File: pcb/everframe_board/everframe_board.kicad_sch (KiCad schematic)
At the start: 4 parts

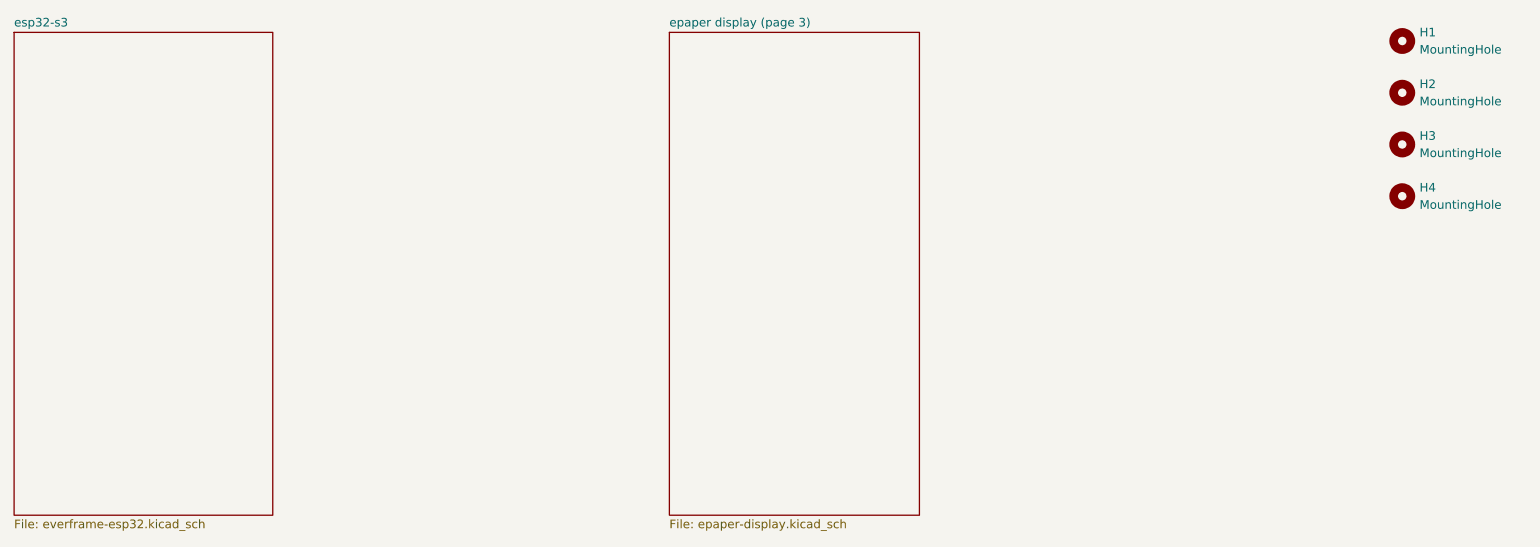
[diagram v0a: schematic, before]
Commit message: Finished sch, started layout 2L only
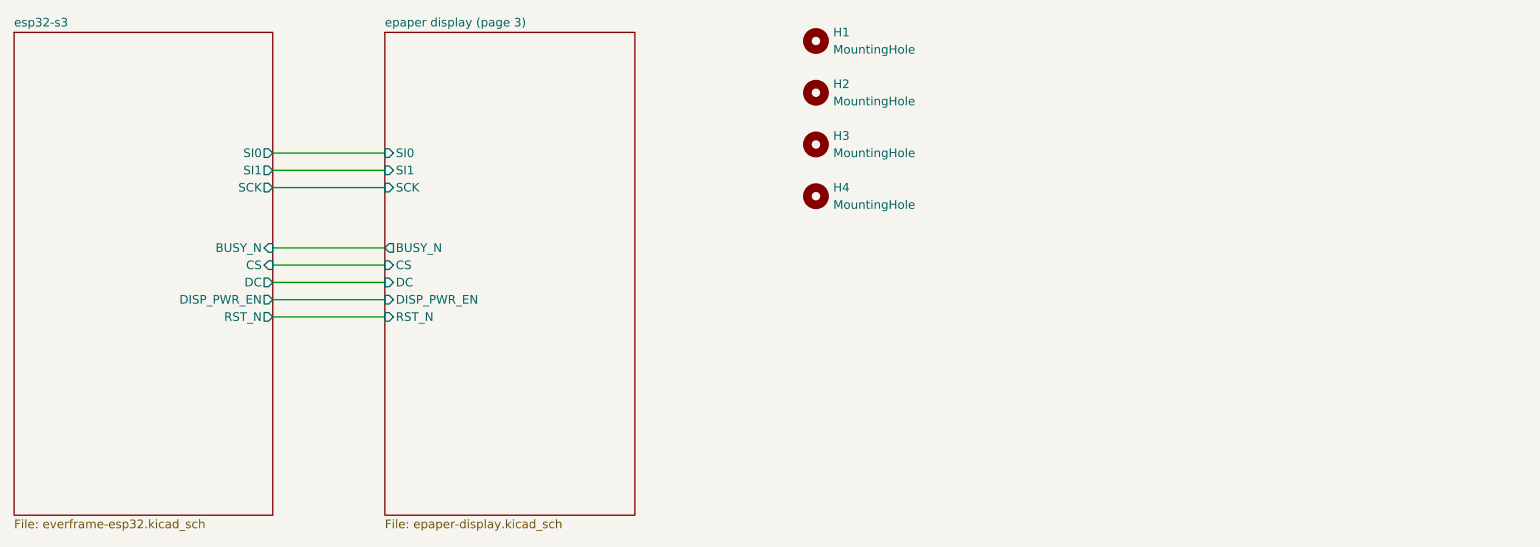
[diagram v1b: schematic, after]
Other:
- sheet epaper display (page 3) ports: added BUSY_N, CS, DC, DISP_PWR_EN, RST_N, SCK, SI0, SI1; removed none
- sheet esp32-s3 ports: added BUSY_N, CS, DC, DISP_PWR_EN, RST_N, SCK, SI0, SI1; removed none
- moved on the sheet: H1, H2, H3, H4
